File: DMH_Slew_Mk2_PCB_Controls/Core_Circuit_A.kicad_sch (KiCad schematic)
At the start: 59 parts, among them J1 TS_Jack_6.35mm_Sw, J11 Conn_02x03_Top_Bottom, J12 Conn_02x06_Top_Bottom, J13 Conn_02x03_Top_Bottom, J14 Conn_02x03_Top_Bottom, J15 Conn_02x06_Top_Bottom, J16 Conn_02x03_Top_Bottom, J17 Conn_01x08, J18 Conn_01x08, J19 Conn_01x08, J2 TS_Jack_6.35mm_Sw, J20 Conn_01x08, J3 TS_Jack_6.35mm_Sw, Q1 BC548, Q2 BC548, Q3 BC558, Q4 BC558, SW1 SW_DPDT_3way, SW2 SW_DPDT, SW3 SPDT_OnOffOn, U1 TL074, U2 TL074

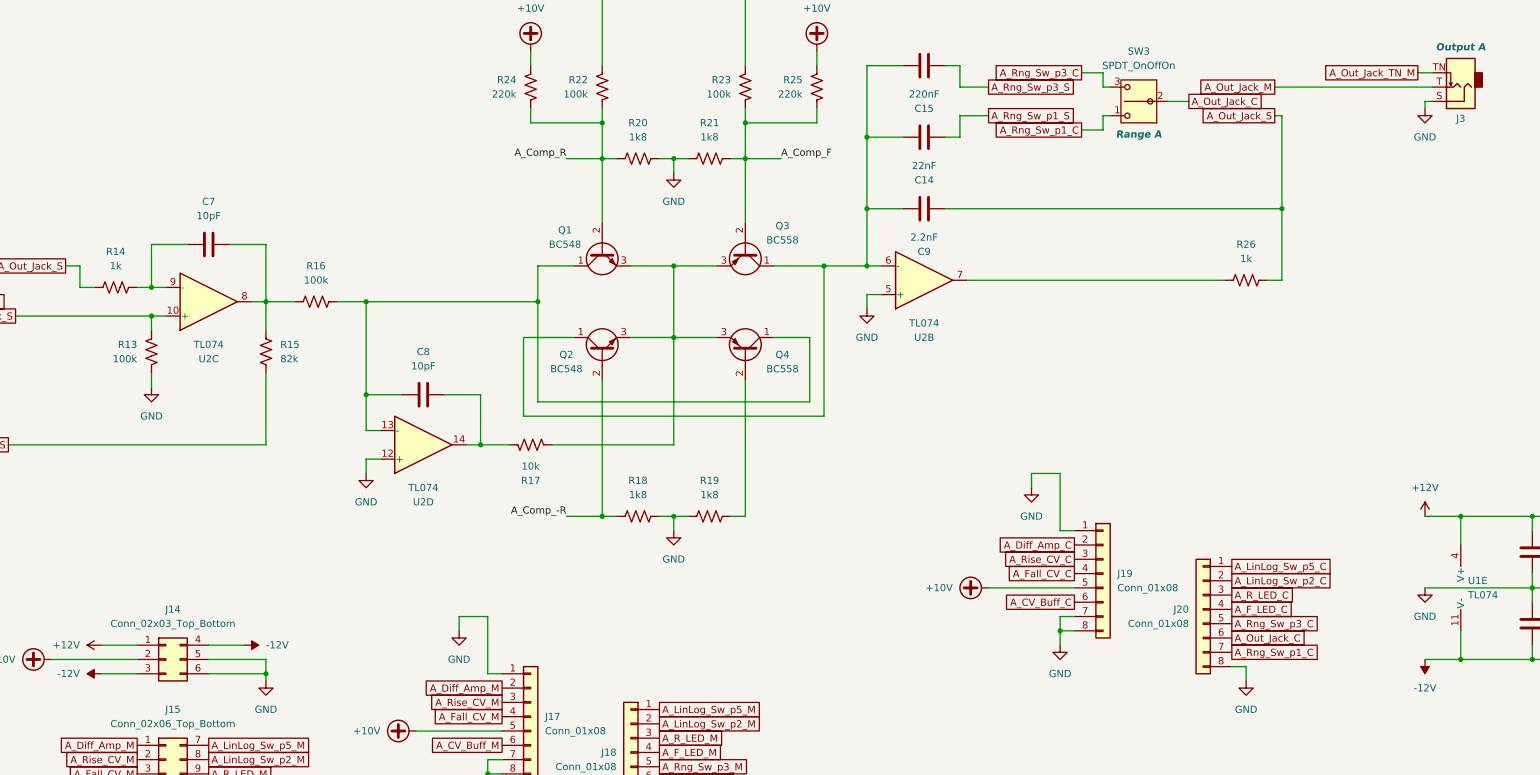
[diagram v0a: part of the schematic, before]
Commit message: Designed Controls PCB
... and removed Mod feature
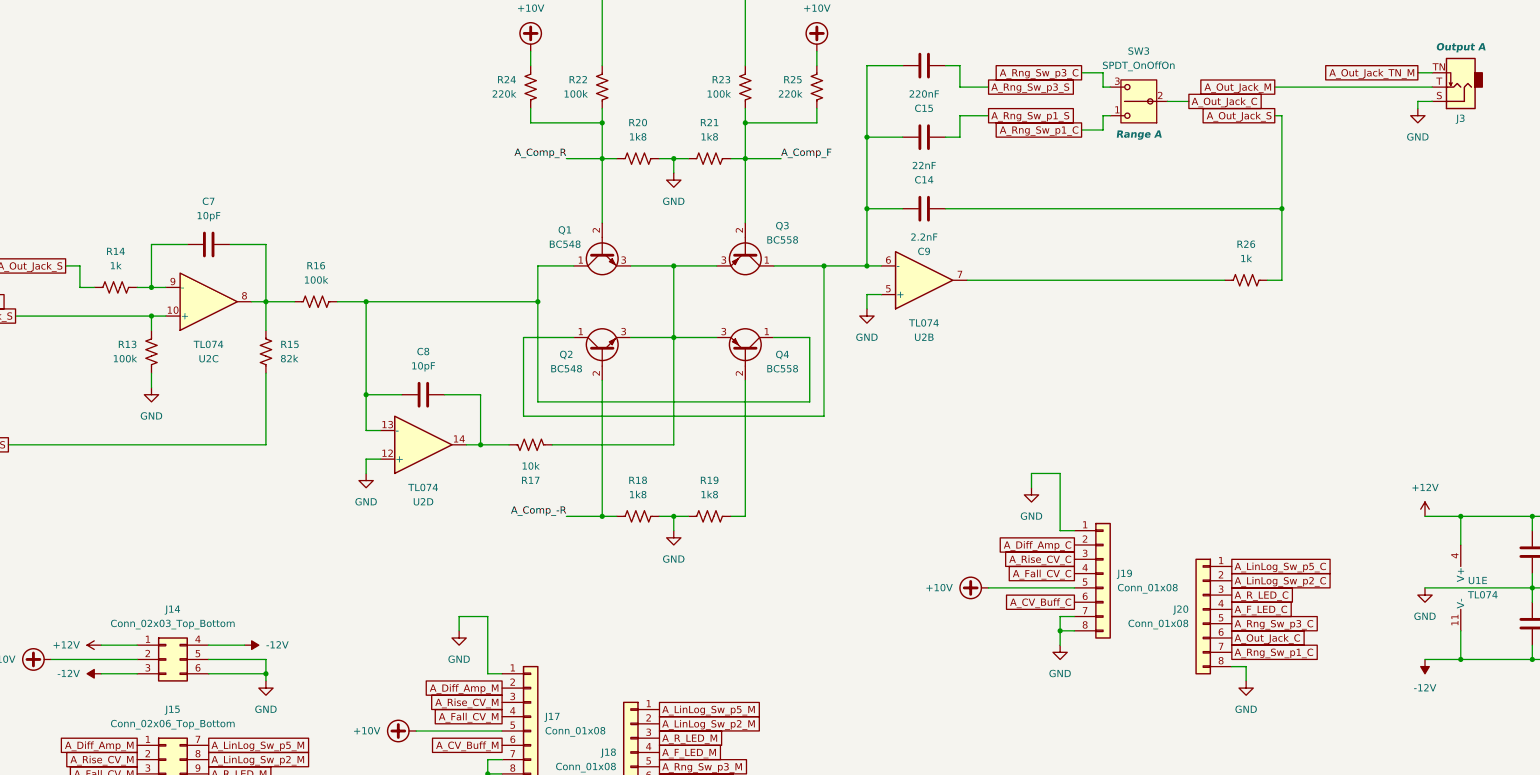
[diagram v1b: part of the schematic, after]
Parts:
- J14, J16: footprint Connector_PinSocket_2.54mm:PinSocket_2x03_P2.54mm_Vertical -> Connector_PinHeader_2.54mm:PinHeader_2x03_P2.54mm_Horizontal
- J15: footprint Connector_PinSocket_2.54mm:PinSocket_2x06_P2.54mm_Vertical -> Connector_PinHeader_2.54mm:PinHeader_2x06_P2.54mm_Horizontal
- J19, J20: footprint Connector_PinHeader_2.54mm:PinHeader_1x08_P2.54mm_Vertical -> Connector_PinSocket_2.54mm:PinSocket_1x08_P2.54mm_Vertical

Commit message: Updated SynthStuff
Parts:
- RV1: footprint Potentiometer_THT:Potentiometer_Alpha_RD902F-40-00D_Dual_Vertical -> SynthStuff:Potentiometer_Alpha_RD902F-40-00D_Dual_Vertical
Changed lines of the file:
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@@
 			)
 		)
-		(property "Footprint" "Potentiometer_THT:Potentiometer_Alpha_RD902F-40-00D_Dual_Vertical"
+		(property "Footprint" "SynthStuff:Potentiometer_Alpha_RD902F-40-00D_Dual_Vertical"
 			(at 167.64 91.44 0)
 			(hide yes)
@@
 			)
 		)
-		(property "Footprint" "Potentiometer_THT:Potentiometer_Alpha_RD902F-40-00D_Dual_Vertical"
+		(property "Footprint" "SynthStuff:Potentiometer_Alpha_RD902F-40-00D_Dual_Vertical"
 			(at 167.64 73.66 0)
 			(hide yes)
